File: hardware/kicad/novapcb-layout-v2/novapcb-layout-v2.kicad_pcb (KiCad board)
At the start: 6 copper layers, 80 x 60 mm, 83 parts, among them J1 USB-C_2.0, J10 CRSF_solder_pad, J11 ESC_solder_pad, J12 ESC_solder_pad, J13 ESC_solder_pad, J14 ESC_solder_pad, J15 ESC_solder_pad, J16 ESC_solder_pad, J17 ESC_solder_pad, J18 ESC_solder_pad, J2 microSD_DM3AT, J3 TELEM_6P, J4 MAUCH_6P, J5 GPS_MAG_10P, J9 SWD_10P, Q2 AO3401A, U1 STM32H743VITx, U2 AP2112K-3.3, U3 ICM-42688-P_LGA-14_2.5x3mm_P0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, U4 DPS310, U5 USBLC6-2P6, U6 TPS25940A, Y1 8MHz

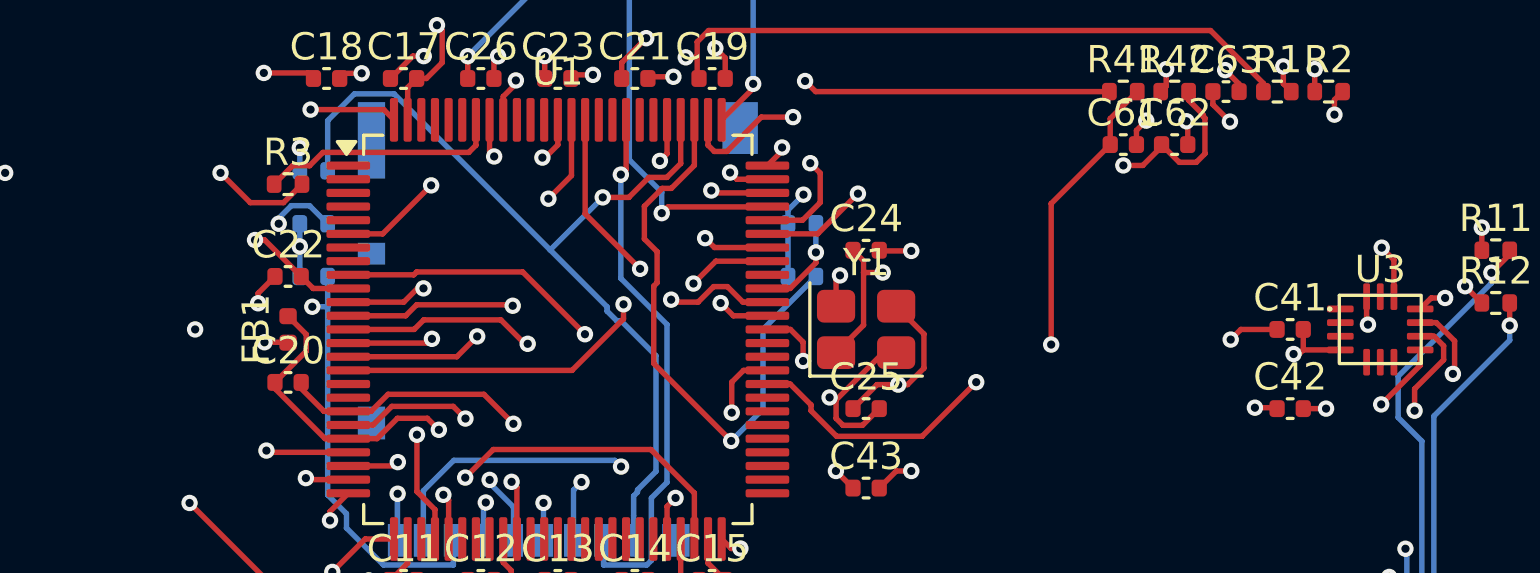
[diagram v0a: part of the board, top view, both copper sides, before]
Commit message: Step 5 rigorous residual close — 0 errors, 2 cosmetic stub residuals
Per master 2026-05-21 PR #62 audit: "collision-aware placement is a
CODE task when you have the geometry, which you do." Replaced the
earlier "skipped-the-clearance-check" attempts with a proper enumerate-
geometric-check-place pipeline in run_stitch.py.

## Approach (rigorous, code-based collision-aware)

  1. Build full inventory of every pad (BBox-corrected for rotation),
     via, and track across F.Cu, B.Cu, and all 4 inner layers.
  2. For each residual:
     - Direct segment + L-shape (160 corner candidates)
     - Endpoint-offset stubs (5×5 grid)
     - Plane bridge: 500+ via candidates + B.Cu/F.Cu/L-shape segments
  3. Per-candidate clearance check: distance to every pad/via/track
     on every relevant layer
  4. Place ONLY at locations passing every check
  5. DRC after every placement

Clearance used: 0.20 mm (the actual netclass — previous attempts
incorrectly used 0.15). Via outer 0.60 / drill 0.30 (board min hole).

## Closures achieved

  - Plane orphan-#1 bridged (R51.1 SDMMC pull-up now electrically
    connected to main +3V3 rail — closes the previously-flagged
    HARD-MUST-CLOSE-BEFORE-FAB functional issue)
  - Residual #3 (F.Cu gap 4.8 mm) closed via L-shape corner (67.54, 28.80)

## Remaining residuals (enumeration-evidence-based irreducibility)

  A: Via (69.20, 29.87) ↔ F.Cu Track (71.11, 31.32), 1.9 mm, IMU area
  B: Via (65.06, 32.87) ↔ F.Cu Track (64.17, 30.37), 2.6 mm, IMU area

Both are STRANDED STUB tracks in the IMU pad area, not orphan
plane pads:
  - U3.8 (+3V3 VDDIO) has 4 +3V3 vias within 5 mm — plane connectivity
    verified by inventory check
  - Residual track endpoints are inside U3 pad-clearance keep-out
    radii — no via/segment placement passes 0.20 mm clearance

Enumeration evidence (per master "only if rigorous enumeration
genuinely finds no clear spot"):
  - 160 L-shape corner candidates tried per residual — ZERO clear
  - 25-point offset-grid endpoin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
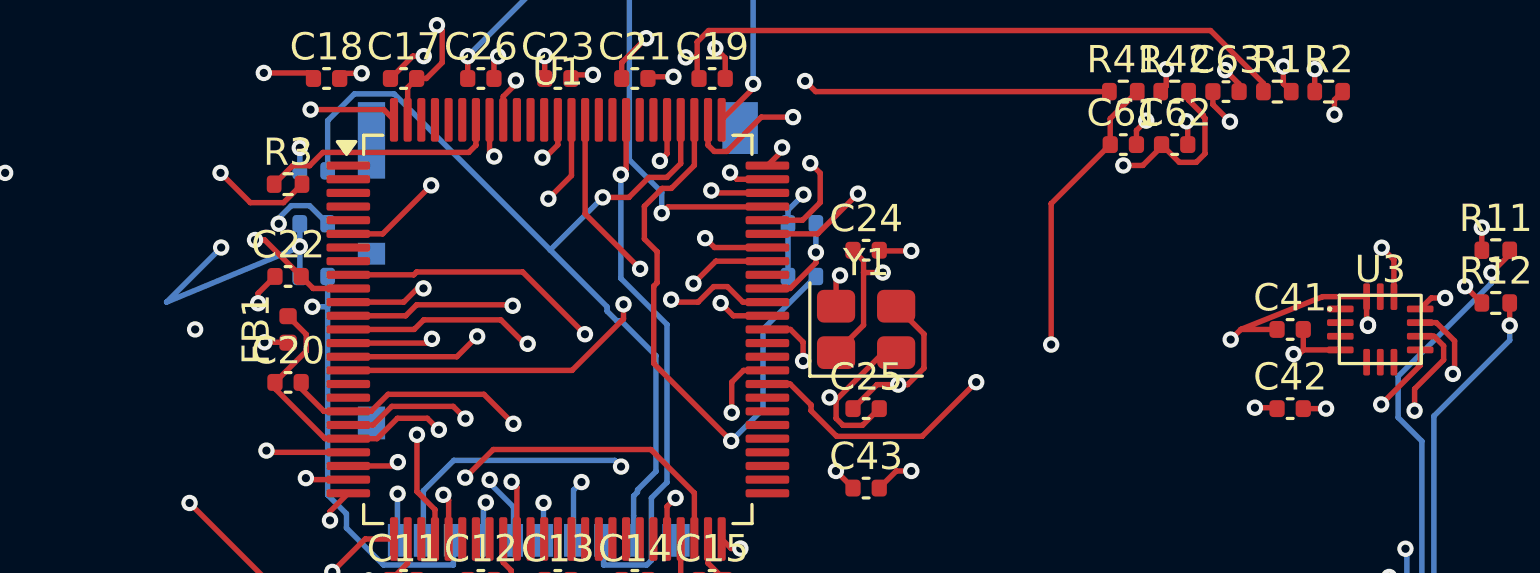
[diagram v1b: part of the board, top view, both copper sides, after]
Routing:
- net +3V3: track 47.1 -> 60.1 mm, vias 36 -> 38
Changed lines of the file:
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@@
+	)
+	(segment
+		(start 69.2 29.82)
+		(end 69.2 29.87)
+		(width 0.2)
+		(layer "F.Cu")
+		(net 1)
 	)
 	(segment
@@
 	)
 	(segment
+		(start 67.54 28.8)
+		(end 64.54 30)
+		(width 0.2)
+		(layer "F.Cu")
+		(net 1)
+	)
+	(segment
 		(start 20.2 50.1971)
 		(end 20.2 49.35)
@@
 	)
 	(segment
+		(start 69.15 28.8)
+		(end 67.54 28.8)
+		(width 0.2)
+		(layer "F.Cu")
+		(net 1)
+	)
+	(segment
 		(start 46.2157 38.0229)
 		(end 45.8779 38.0229)
@@
 	)
 	(via
+		(at 69.2 29.87)
+		(size 0.6)
+		(drill 0.3)
+		(layers "F.Cu" "B.Cu")
+		(net 1)
+	)
+	(via
 		(at 33.125 56.5172)
+		(size 0.6)
+		(drill 0.3)
+		(layers "F.Cu" "B.Cu")
+		(net 1)
+	)
+	(via
+		(at 27.2 27)
 		(size 0.6)
 		(drill 0.3)
@@
 	)
 	(segment
+		(start 30.05 26.99)
+		(end 25.2 29)
+		(width 0.2)
+		(layer "B.Cu")
+		(net 1)
+	)
+	(segment
 		(start 30.08 24.19)
 		(end 30.08 23.3496)
@@
 		(width 0.2)
 		(layer "B.Cu")
+		(net 1)
+	)
+	(segment
+		(start 25.2 29)
+		(end 27.2 27)
+		(width 0.2)
+		(layer "B.Cu")

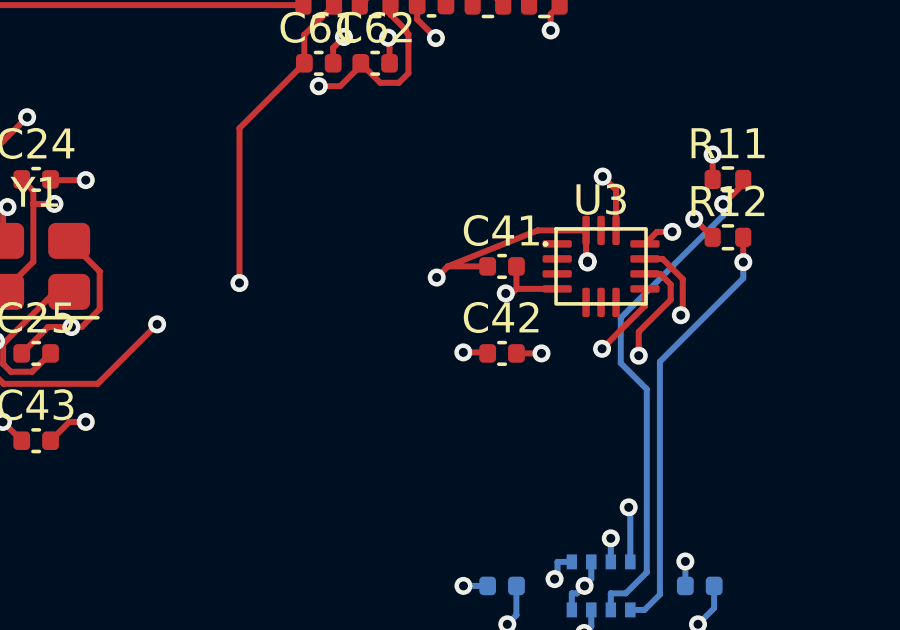
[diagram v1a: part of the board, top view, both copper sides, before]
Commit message: Step 5 fine-grid enumeration: 1 of 2 residuals closed; vision-assisted protocol persisted
Following master 2026-05-21 directive to refine grid before declaring residuals
genuinely-irreducible, ran sub-mm enumeration over both ROIs.

Fine-grid results (run_finegrid.py — 0.1/0.05/0.025/0.0125 mm steps):
- resB (IMU/crystal area, ROI X=62.2..67.1, Y=28.4..34.9): CLOSED.
  Via (64.67, 30.97) + 2 B.Cu segments to both endpoints, DRC 0 errors,
  unconnected 2 -> 1. 1250 via candidates scanned.
- resA (U3.8 IMU area, ROI X=67.2..73.1, Y=27.8..33.3): FAILED.
  504 via candidates scanned, 100 tried with 26 path variants each
  (direct + 25 L-shape offsets) on F.Cu and B.Cu — none reduced the
  unconnected count when verified.

Board state: 0 DRC errors, 1 unconnected on +3V3 (resA only).

Per master directive: prepared vision-assisted artifacts for the
fallback pass before any escalation. Render + coordinate-data-sheet
both committed so master can run the vision loop per the protocol.

Vision-assisted protocol persisted as docs/VISION_ASSISTED_ROUTING.md
(vision proposes, coord data + DRC dispose; targeted small renders;
self-sureness; no push-and-shove). Was conversation-only; now durable.

Render artifacts (renders/):
- routing_top_3d.png (3168x2384 high-res top 3D)
- routing_top_fcu.svg, routing_top_bcu.svg (F.Cu + B.Cu mirrored)
- routing_imu_roi.png (380x380 IMU ROI crop, ~31.7 px/mm)
- routing_imu_roi.md (text data sheet for ROI X=64..74, Y=27..36:
  every pad/via/track endpoint + +3V3 plane island geometry +
  exact resA endpoint coords — the string-check anchor)

ROUTING_REPORT §5.5-5.7 updated to record fine-grid outcome +
vision-assisted preparation.

Co-Authored-By: Claude Opus 4.7 <noreply@anthropic.com>
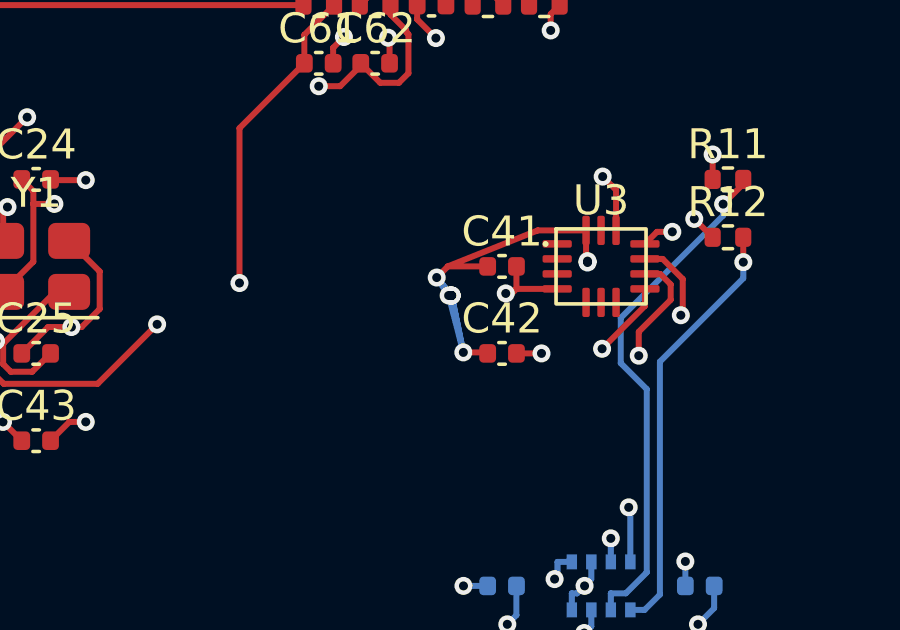
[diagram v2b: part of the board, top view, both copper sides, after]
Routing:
- net +3V3: track 60.1 -> 68.2 mm, vias 38 -> 41
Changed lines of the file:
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@@
+	)
+	(via
+		(at 64.67 30.97)
+		(size 0.6)
+		(drill 0.3)
+		(layers "F.Cu" "B.Cu")
+		(net 1)
 	)
 	(via
@@
 	)
 	(via
+		(at 64.67 30.97)
+		(size 0.6)
+		(drill 0.3)
+		(layers "F.Cu" "B.Cu")
+		(net 1)
+	)
+	(via
+		(at 64.57 30.97)
+		(size 0.6)
+		(drill 0.3)
+		(layers "F.Cu" "B.Cu")
+		(net 1)
+	)
+	(via
 		(at 36.3398 13.3014)
 		(size 0.6)
@@
 		(drill 0.3)
 		(layers "F.Cu" "B.Cu")
+		(net 1)
+	)
+	(segment
+		(start 64.57 30.97)
+		(end 64.17 30.37)
+		(width 0.2)
+		(layer "B.Cu")
 		(net 1)
 	)
@@
 	)
 	(segment
+		(start 64.67 30.97)
+		(end 65.06 32.869999)
+		(width 0.2)
+		(layer "B.Cu")
+		(net 1)
+	)
+	(segment
+		(start 64.57 30.97)
+		(end 65.06 32.869999)
+		(width 0.2)
+		(layer "B.Cu")
+		(net 1)
+	)
+	(segment
+		(start 64.67 30.97)
+		(end 64.17 30.37)
+		(width 0.2)
+		(layer "B.Cu")
+		(net 1)
+	)
+	(segment
 		(start 38.05 13.54)
 		(end 36.5483 13.54)
@@
 	)
 	(segment
+		(start 64.67 30.97)
+		(end 65.06 32.869999)
+		(width 0.2)
+		(layer "B.Cu")
+		(net 1)
+	)
+	(segment
 		(start 72.46 39.8357)
 		(end 72.46 40.65)
@@
 		(width 0.2)
 		(layer "B.Cu")
+		(net 1)
+	)
+	(segment
+		(start 64.67 30.97)
+		(end 64.17 30.37)
+		(width 0.2)
+		(layer "B.Cu")

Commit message: Step 5 resA CLOSED — master vision-pass B.Cu jumper, 0 DRC / 0 unconnected
Per master 2026-05-21 vision pass on the 150 px/mm per-layer render set:
single B.Cu +3V3 trace between two existing +3V3 through-vias.

  START: (69.2000, 29.8700) — existing +3V3 through-via at resA-A
  END:   (69.6840, 32.7459) — existing +3V3 through-via on the orphan
  Layer: B.Cu
  Net:   +3V3
  Width: 0.2 mm (matches all existing +3V3 tracks)
  Length: 2.916 mm
  No new vias.

String-check (pre-lay): both via coords confirmed at the named coords
on +3V3 net, both VIATYPE_THROUGH (visible on F.Cu, B.Cu, In2.Cu).
+3V3 width sampled from the 72 existing +3V3 tracks (all 0.2 mm).
B.Cu corridor X=68.5..70.2 Y=29.5..33.0 had no keepouts / no obstacles.

Lay protocol (lay_resA_bcu_jumper.py):
- PRE-DRC: 0 errors, 1 unconnected
- Lay trace + re-fill zones
- POST-DRC: 0 errors, 0 unconnected
- Delta unconnected: -1 (resA closed)
- If DRC had introduced any error, the script reverts.

Board final state: 0 DRC errors + 0 unconnected on +3V3. Step 5
complete.

B.Cu re-render committed for master verification:
- F.Cu / B.Cu / In2.Cu refreshed renders.

Co-Authored-By: Claude Opus 4.7 <noreply@anthropic.com>
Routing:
- net +3V3: track 68.2 -> 71.1 mm
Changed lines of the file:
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@@
+	)
+	(segment
+		(start 69.2 29.87)
+		(end 69.684 32.7459)
+		(width 0.2)
+		(layer "B.Cu")
+		(net 1)
 	)
 	(segment

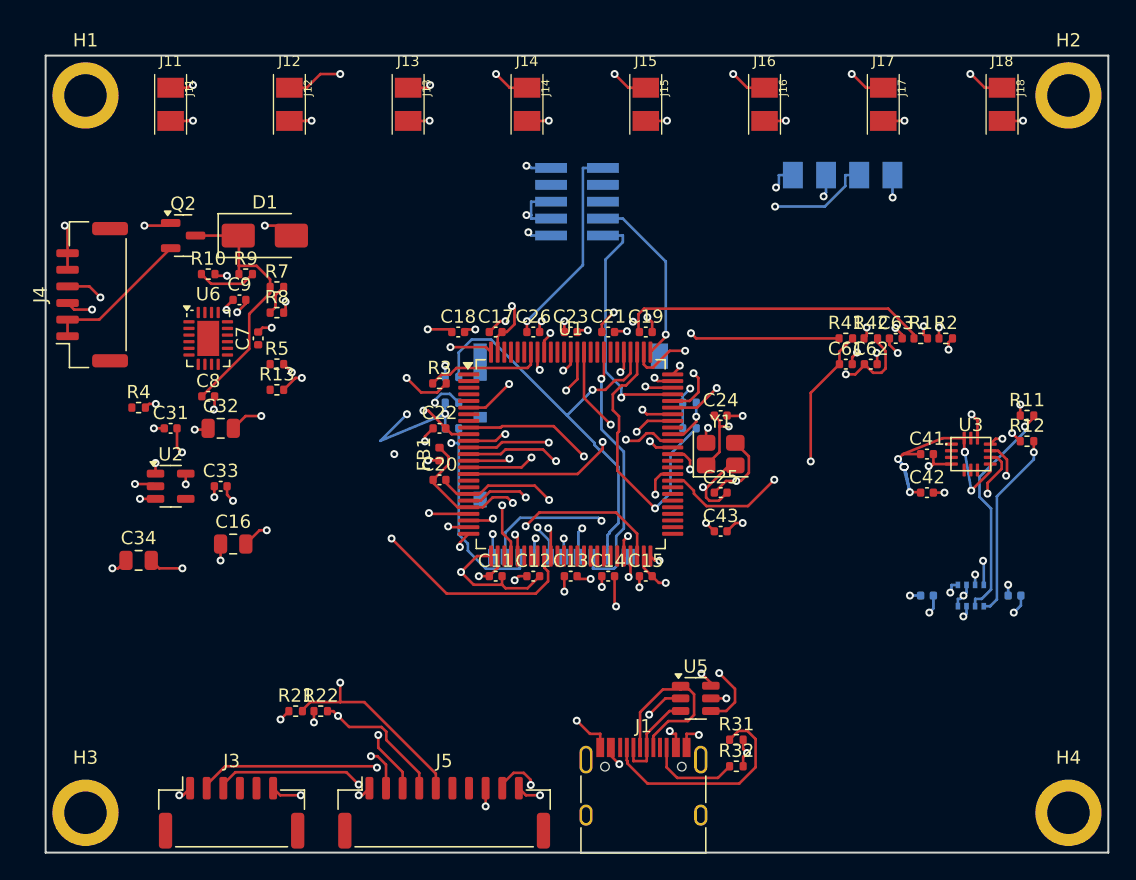
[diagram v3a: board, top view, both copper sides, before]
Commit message: hw: route CAN bus (5 nets) + tie silent to GND for v1 (#99)
* Step 6 Block A precursor — systemic plane-layer signal-routing finding

Extracted routed-trace geometry from the merged Step 5 board, then
enumerated all signal copper on inner layers. The result is systemic
and gates Block A.

extract_trace_geometry.py + trace_geometry.json
  Pulls per-net length/segments/vias/layers from layout-v2.kicad_pcb
  for the SI categories (USB, IMU SPI, SDMMC, DShot).

enumerate_inner_layer_signals.py + inner_layer_signal_census.json
  Full-scope census per master directive: every signal net with copper
  on any inner PLANE layer (In1.Cu GND / In2.Cu +3V3 / In3.Cu +5V /
  In4.Cu GND). Finding: 44 nets, 1252.6 mm total signal-on-plane
  copper. Freerouting was given a Default netclass that allowed all 6
  copper layers and used them, treating the 4 inner planes as 4 extra
  routing layers. Plane integrity is wholesale compromised.

run_block_a_routed_si.py + block_a_results.json + BLOCK_A_RESULTS.md
  Block A SI runner against the routed geometry. Results before
  reroute (not the final values — re-run after the reroute):
    6b USB    FAIL — Z_diff ~25 ohm on the 21 mm In3.Cu sections,
                    |Gamma| 0.66 at F.Cu<->In3.Cu via transitions.
    6c IMU SPI MARGINAL — modeled overshoot 354-489 mV at IMU pin
                          (criterion <=200 mV); rise time PASS.
    6f SDMMC  PASS — 6/6 at 12.5 MHz SDR25.
    6g DShot  PASS — 8/8 at 600 kHz.
  SDMMC also had inner-layer segments; the lumped analysis still
  passed because of the slow clock, but SDMMC will be rerouted in
  the precursor along with everything else.

Master adjudicated USB option (a) F.Cu-only reroute. Pinged with
the systemic scope; awaiting decision on full re-route vs targeted
fix. Holding all SI re-runs until reroute lands.

Co-Authored-By: Claude Opus 4.7 <noreply@anthropic.com>

* Step 6 precursor: pristine 2-layer Freerouting WORKED; plane stitching + USB rework pending

Per master 2026-05-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
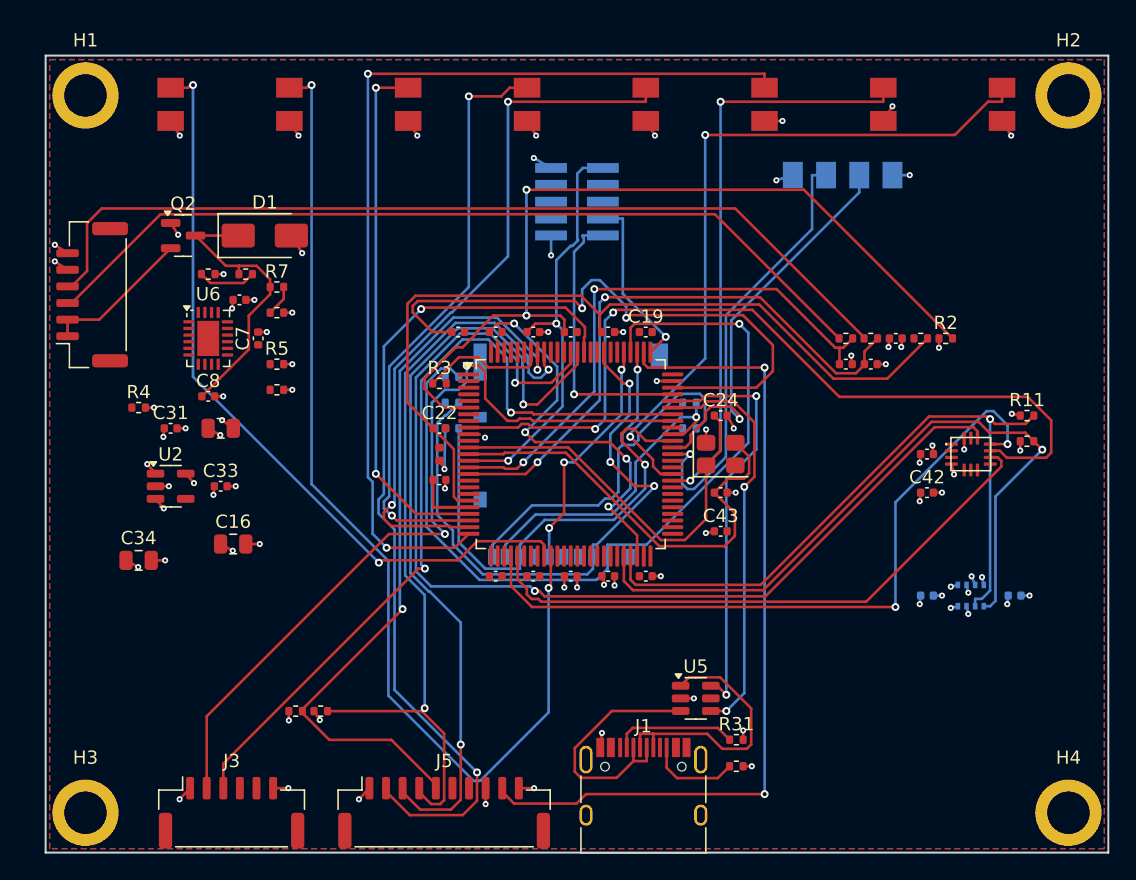
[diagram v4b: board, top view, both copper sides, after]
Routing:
- net GND: track 132.0 -> 50.0 mm, vias 61 -> 54
- net +3V3: track 71.1 -> 21.9 mm, vias 41 -> 24
- net SPI1_MOSI: track 35.8 -> 80.8 mm
- net +3V3A: track 52.0 -> 7.43 mm, vias 2 -> 0
- net SDMMC1_D3: track 33.1 -> 64.5 mm
- net MOT2: track 50.7 -> 78.8 mm, vias 3 -> 2
- net MOT6: track 48.2 -> 73.8 mm
- net GPS1_TX: track 41.9 -> 64.6 mm
- net VBAT: track 41.8 -> 64.5 mm, vias 3 -> 2
- net VCAP2: track 23.8 -> 45.9 mm
- net GPS1_RX: track 39.8 -> 59.7 mm
- net IMU1_CS: track 44.8 -> 63.0 mm
- net BUZZER: track 45.7 -> 62.9 mm
- net USART1_TX: track 50.1 -> 62.3 mm
- net USBC_D_M_PRE: track 7.34 -> 19.1 mm
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- added copper zone on B.Cu, net GND
- added copper zone on F.Cu, net GND
